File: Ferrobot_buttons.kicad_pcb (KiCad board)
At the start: 2 copper layers, 83.8 x 63.5 mm, 16 parts, among them J1 CONN_02X06, J2 CONN_01X01, J3 CONN_01X01, J4 CONN_01X01, J5 CONN_01X01, SW1 Button, SW10 SW_DIP_x01, SW2 Button, SW3 Button, SW4 Button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

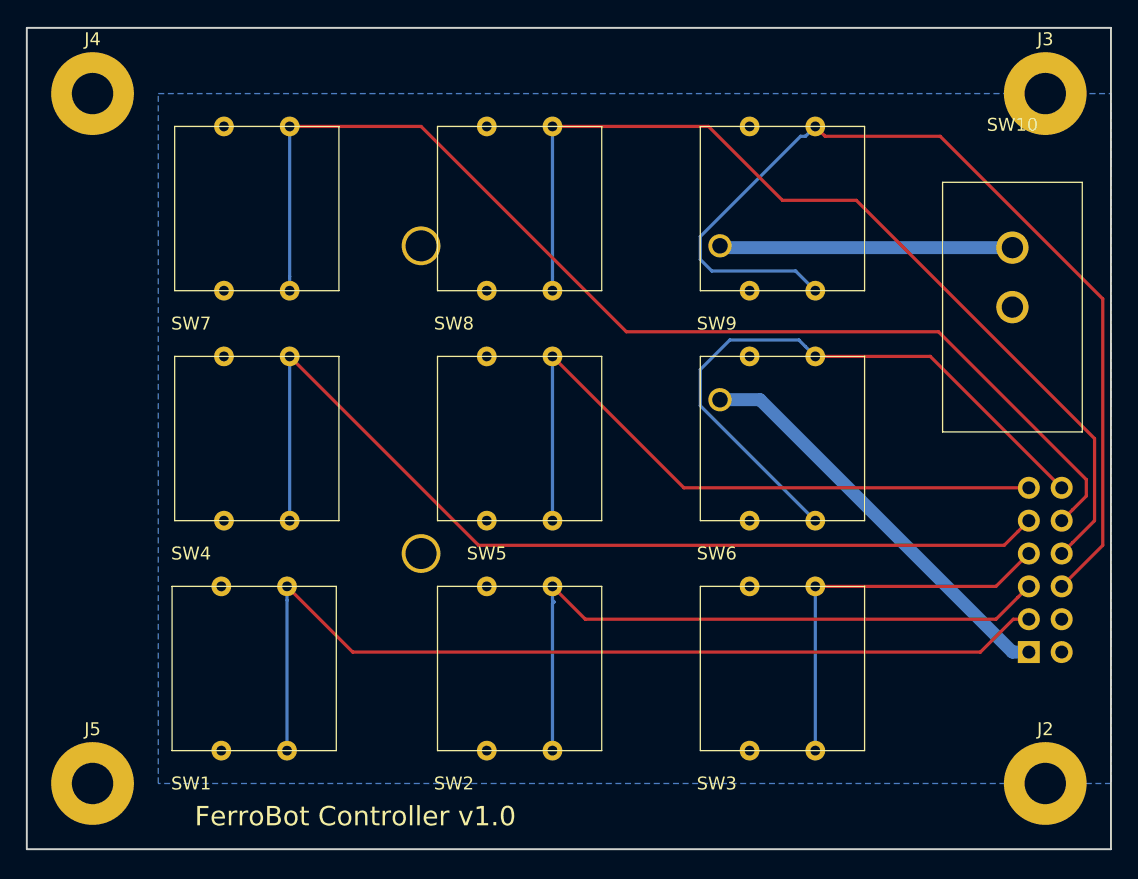
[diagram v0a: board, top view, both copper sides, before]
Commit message: Add pul-down resistors
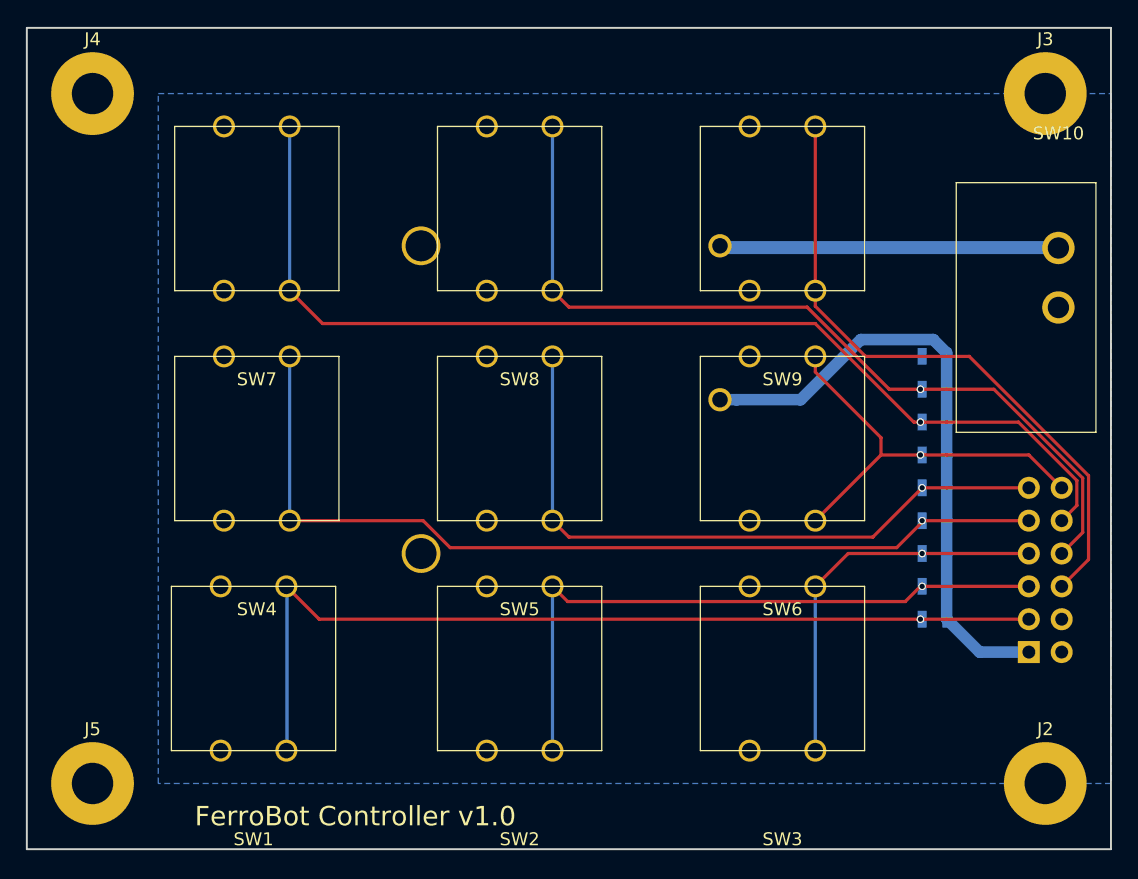
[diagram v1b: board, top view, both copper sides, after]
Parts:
- added R1: 10k, Resistors_SMD:R_0805, B.Cu at (138.8, 157.5)
- added R2: 10k, Resistors_SMD:R_0805, B.Cu at (138.8, 154.9)
- added R3: 10k, Resistors_SMD:R_0805, B.Cu at (138.8, 152.4)
- added R4: 10k, Resistors_SMD:R_0805, B.Cu at (138.8, 149.9)
- added R5: 10k, Resistors_SMD:R_0805, B.Cu at (138.8, 147.3)
- added R6: 10k, Resistors_SMD:R_0805, B.Cu at (138.7, 137.2)
- added R7: 10k, Resistors_SMD:R_0805, B.Cu at (138.7, 139.7)
- added R8: 10k, Resistors_SMD:R_0805, B.Cu at (138.7, 142.2)
- added R9: 10k, Resistors_SMD:R_0805, B.Cu at (138.8, 144.8)
- moved SW10 3.56 mm to (148.3, 123.7)
- moved SW1 0.05 mm to (86.1, 167.6)
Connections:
- J1 pad 4: Net-(J1-Pad4) -> (no net)
- J2 pad 1: Net-(J2-Pad1) -> (no net)
- J3 pad 1: Net-(J3-Pad1) -> (no net)
- J4 pad 1: Net-(J4-Pad1) -> (no net)
- J5 pad 1: Net-(J5-Pad1) -> (no net)
- SW1 pad 3: MAGNET1 -> PWR
- SW1 pad 4: PWR -> MAGNET1
- SW2 pad 3: MAGNET2 -> PWR
- SW2 pad 4: PWR -> MAGNET2
- SW3 pad 3: MAGNET3 -> PWR
- SW3 pad 4: PWR -> MAGNET3
- SW4 pad 3: MAGNET4 -> PWR
- SW4 pad 4: PWR -> MAGNET4
- SW5 pad 3: MAGNET5 -> PWR
- SW5 pad 4: PWR -> MAGNET5
- SW6 pad 3: MAGNET6 -> PWR
- SW6 pad 4: PWR -> MAGNET6
- SW7 pad 3: MAGNET7 -> PWR
- SW7 pad 4: PWR -> MAGNET7
- SW8 pad 3: MAGNET8 -> PWR
- SW8 pad 4: PWR -> MAGNET8
- SW9 pad 3: MAGNET9 -> PWR
- SW9 pad 4: PWR -> MAGNET9
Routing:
- net MAGNET9: track 75.4 -> 49.9 mm
- net MAGNET6: track 49.0 -> 31.9 mm, vias 0 -> 1
- net GND: track 32.0 -> 48.2 mm
- net MAGNET8: track 74.5 -> 66.2 mm, vias 0 -> 1
- net MAGNET7: track 89.6 -> 83.5 mm, vias 0 -> 1
- net MAGNET4: track 76.7 -> 71.7 mm, vias 0 -> 1
- net BATTERY_OUT: track 22.5 -> 26.0 mm
- net MAGNET5: track 53.7 -> 51.6 mm, vias 0 -> 1
- net MAGNET1: track 73.2 -> 71.2 mm, vias 0 -> 1
- net MAGNET2: track 51.7 -> 50.6 mm, vias 0 -> 1
- net MAGNET3: vias 0 -> 1
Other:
- net class LARGE added: clearance 0.2, trace_width 0.9, via_dia 0.6, via_drill 0.4
